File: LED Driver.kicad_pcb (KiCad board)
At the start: 2 copper layers, 15 x 15 mm, 9 parts, among them J1 CONN_01X02, J2 CONN_01X03, J3 GS3, U1 NCP5006

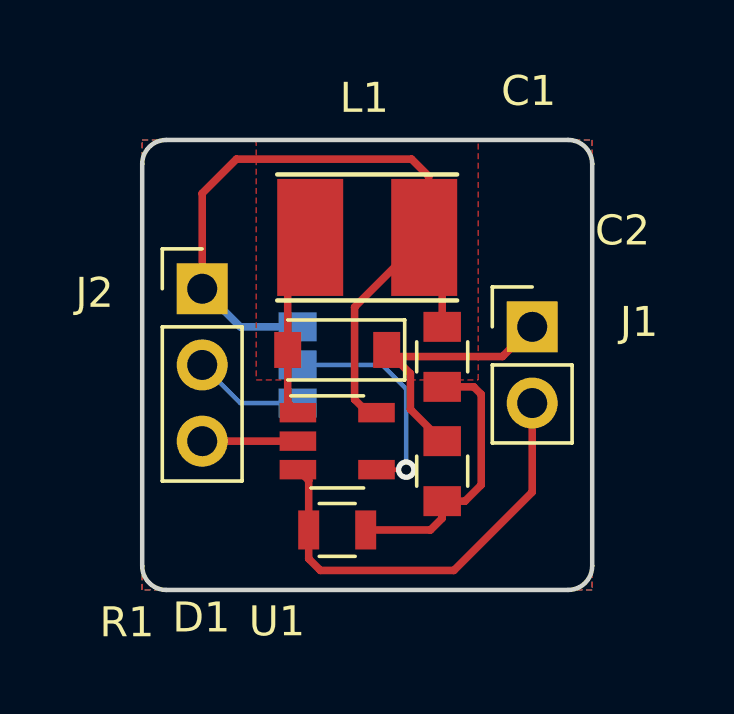
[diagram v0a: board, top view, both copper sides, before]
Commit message: Added labels and component references to Silkscreen
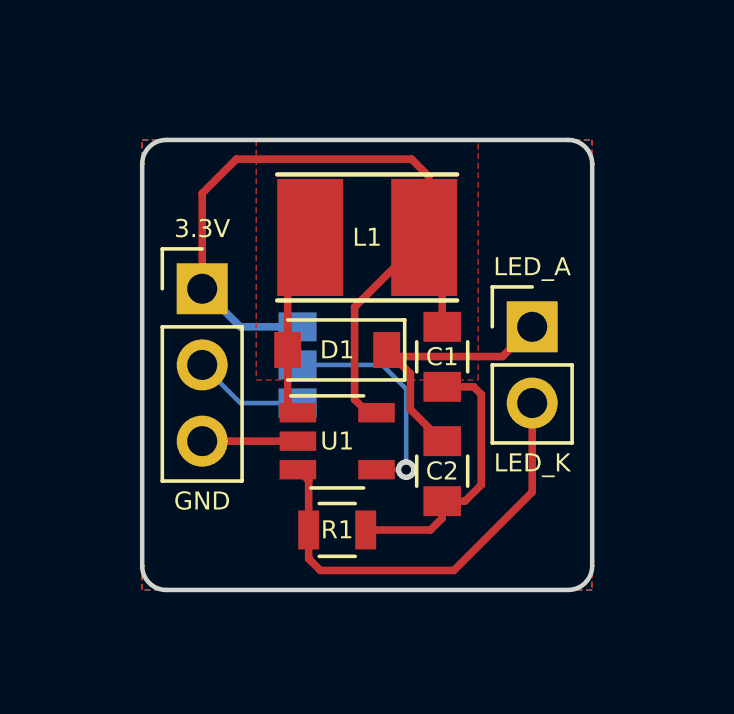
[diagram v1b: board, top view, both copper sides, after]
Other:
- board text added: "3.3V"
- board text added: "EN"
- board text added: "EN_CONN"
- board text added: "GND"
- board text added: "LED_A"
- board text added: "LED_K"
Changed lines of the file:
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@@
     (links 16)
     (no_connects 0)
-    (area 96.912667 82.341 118.087334 102.209)
+    (area 99.924999 84.924999 115.075001 100.075001)
     (thickness 1.6)
-    (drawings 8)
+    (drawings 15)
     (tracks 45)
     (zones 0)
@@
     (tags "capacitor 0805")
     (attr smd)
-    (fp_text reference C2 (at -8.02 -6.01 360) (layer F.SilkS)
-      (effects (font (size 1 1) (thickness 0.15)))
+    (fp_text reference C2 (at 0 0 360) (layer F.SilkS)
+      (effects (font (size 0.6 0.6) (thickness 0.15)))
     )
     (fp_text value 1uF (at 0 1.75 270) (layer F.Fab)
@@
     (tags "capacitor 0805")
     (attr smd)
-    (fp_text reference C1 (at -8.86 -2.88 360) (layer F.SilkS)
-      (effects (font (size 1 1) (thickness 0.15)))
+    (fp_text reference C1 (at 0 0 360) (layer F.SilkS)
+      (effects (font (size 0.6 0.6) (thickness 0.15)))
     )
     (fp_text value 4.7uF (at 0 1.75 270) (layer F.Fab)
@@
     (descr "Through hole straight pin header, 1x02, 2.54mm pitch, single row")
     (tags "Through hole pin header THT 1x02 2.54mm single row")
-    (fp_text reference J1 (at 3.56 -0.16) (layer F.SilkS)
+    (fp_text reference J1 (at 3.56 -0.16) (layer F.SilkS) hide
       (effects (font (size 1 1) (thickness 0.15)))
     )
@@
     (tags "inductor taiyo-yuden nr smd")
     (attr smd)
-    (fp_text reference L1 (at 0.1 4.65 180) (layer F.SilkS)
-      (effects (font (size 1 1) (thickness 0.15)))
+    (fp_text reference L1 (at 0 0 180) (layer F.SilkS)
+      (effects (font (size 0.6 0.6) (thickness 0.15)))
     )
     (fp_text value 22uH (at -0.05 -4.66 180) (layer F.Fab)
@@
     (tags "resistor 0805")
     (attr smd)
-    (fp_text reference R1 (at -7.01 3.08) (layer F.SilkS)
-      (effects (font (size 1 1) (thickness 0.15)))
+    (fp_text reference R1 (at 0 0) (layer F.SilkS)
+      (effects (font (size 0.6 0.6) (thickness 0.15)))
     )
     (fp_text value 5.1 (at 0 1.75) (layer F.Fab)
@@
     (descr "Through hole straight pin header, 1x03, 2.54mm pitch, single row")
     (tags "Through hole pin header THT 1x03 2.54mm single row")
-    (fp_text reference J2 (at -3.59 0.14 180) (layer F.SilkS)
+    (fp_text reference J2 (at -3.59 0.14) (layer F.SilkS) hide
       (effects (font (size 1 1) (thickness 0.15)))
     )
@@
     (tags SOD-123)
     (attr smd)
-    (fp_text reference D1 (at 4.53 -8.92 180) (layer F.SilkS)
-      (effects (font (size 1 1) (thickness 0.15)))
+    (fp_text reference D1 (at 0 0 180) (layer F.SilkS)
+      (effects (font (size 0.6 0.6) (thickness 0.15)))
     )
     (fp_text value MBR0530 (at 0 2.1 180) (layer F.Fab)
@@
     (tags TSOT-23-5)
     (attr smd)
-    (fp_text reference U1 (at -2.01 6.01) (layer F.SilkS)
-      (effects (font (size 1 1) (thickness 0.15)))
+    (fp_text reference U1 (at 0 0) (layer F.SilkS)
+      (effects (font (size 0.6 0.6) (thickness 0.15)))
     )
     (fp_text value NCP5006 (at 0 2.5) (layer F.Fab)
@@
     )
   )
+  (gr_text EN_CONN (at 106.2 93.77) (layer B.SilkS)
+    (effects (font (size 0.6 0.6) (thickness 0.15)) (justify right mirror))
+  )
+  (gr_text EN (at 106.2 92.5) (layer B.SilkS)
+    (effects (font (size 0.6 0.6) (thickness 0.15)) (justify right mirror))
+  )
+  (gr_text 3.3V (at 106.2 91.23) (layer B.SilkS)
+    (effects (font (size 0.6 0.6) (thickness 0.15)) (justify right mirror))
+  )
+  (gr_text GND (at 102 97.04) (layer F.SilkS)
+    (effects (font (size 0.6 0.6) (thickness 0.15)))
+  )
+  (gr_text 3.3V (at 102 87.96) (layer F.SilkS)
+    (effects (font (size 0.6 0.6) (thickness 0.15)))
+  )
+  (gr_text LED_K (at 113 95.77) (layer F.SilkS)
+    (effects (font (size 0.6 0.6) (thickness 0.15)))
+  )
+  (gr_text LED_A (at 113 89.23) (layer F.SilkS)
+    (effects (font (size 0.6 0.6) (thickness 0.15)))
+  )
   (gr_arc (start 114.2 99.2) (end 115 99.2) (angle 90) (layer Edge.Cuts) (width 0.15))

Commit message: Adds project name and version (v1.0) to silkscreen
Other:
- board text added: "LED Driver - NCP5006"
- board text added: "v1.0"
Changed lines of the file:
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@@
     (area 99.924999 84.924999 115.075001 100.075001)
     (thickness 1.6)
-    (drawings 15)
+    (drawings 17)
     (tracks 45)
     (zones 0)
@@
     )
   )
+  (gr_text v1.0 (at 102 98) (layer B.SilkS)
+    (effects (font (size 0.8 0.8) (thickness 0.18)) (justify mirror))
+  )
+  (gr_text "LED Driver - NCP5006" (at 107.5 87.25) (layer B.SilkS)
+    (effects (font (size 0.8 0.8) (thickness 0.18)) (justify mirror))
+  )
   (gr_text EN_CONN (at 106.2 93.77) (layer B.SilkS)
